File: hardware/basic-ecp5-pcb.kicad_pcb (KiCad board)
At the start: 4 copper layers, 100 x 68 mm, 75 parts, among them J1 Conn_01x02, J10 Conn_02x05_Odd_Even, J2 Conn_02x20_Odd_Even, J3 Conn_02x06_Odd_Even, J4 Conn_02x06_Odd_Even, J5 Conn_02x06_Odd_Even, J6 Conn_02x06_Odd_Even, J7 Conn_02x06_Odd_Even, J8 Conn_02x06_Odd_Even, J9 Conn_02x20_Odd_Even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

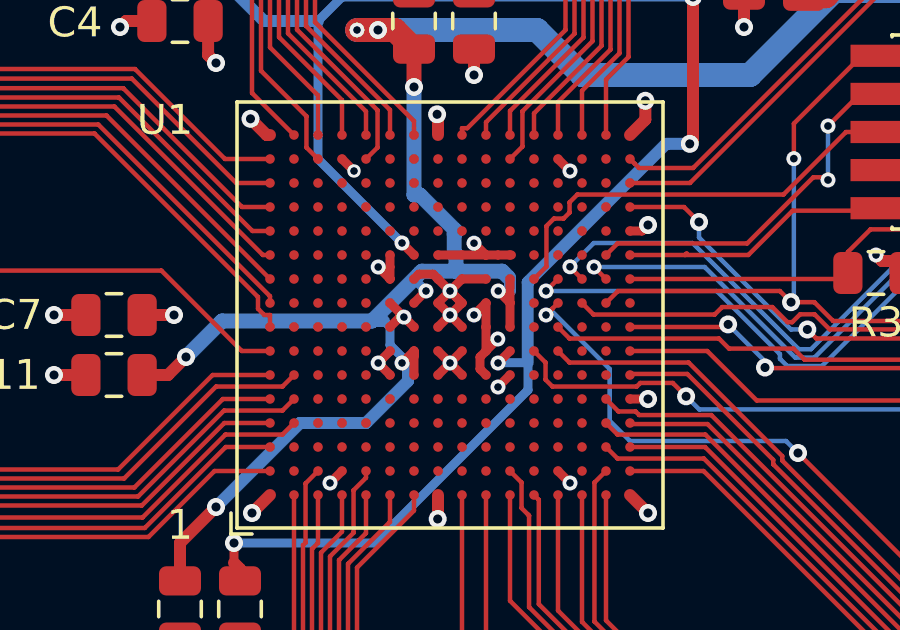
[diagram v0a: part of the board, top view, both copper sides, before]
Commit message: Fanout BGA center
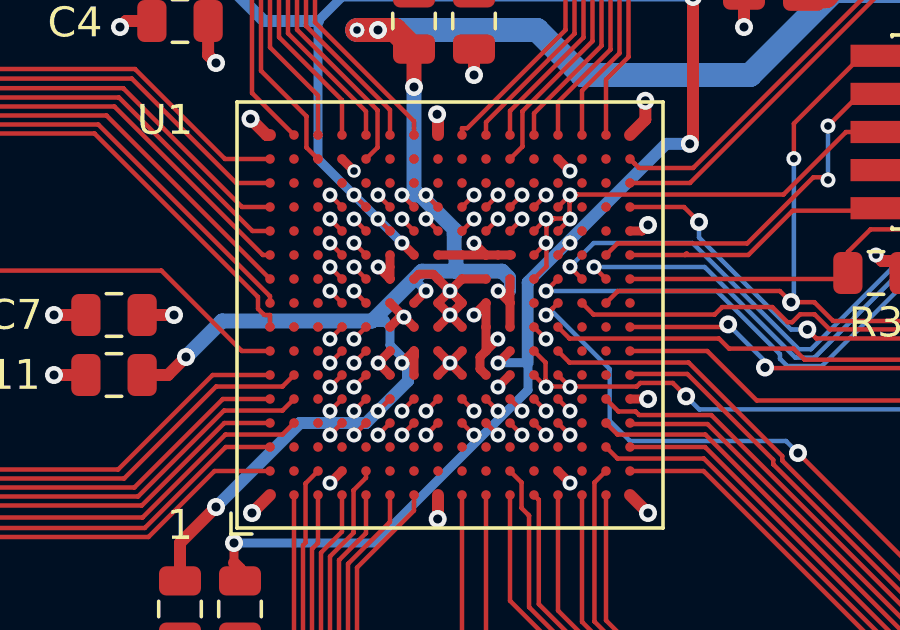
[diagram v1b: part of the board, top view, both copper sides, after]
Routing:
- net Net-(U1-PadN6): track 0.00 -> 0.57 mm, vias 0 -> 1
- net Net-(U1-PadN5): track 0.00 -> 0.57 mm, vias 0 -> 1
- net Net-(U1-PadN4): track 0.00 -> 0.57 mm, vias 0 -> 1
- net Net-(U1-PadN13): track 0.00 -> 0.57 mm, vias 0 -> 1
- net Net-(U1-PadN12): track 0.00 -> 0.57 mm, vias 0 -> 1
- net Net-(U1-PadN11): track 0.00 -> 0.57 mm, vias 0 -> 1
- net Net-(U1-PadM6): track 0.00 -> 0.57 mm, vias 0 -> 1
- net Net-(U1-PadM5): track 0.00 -> 0.57 mm, vias 0 -> 1
- net Net-(U1-PadM4): track 0.00 -> 0.57 mm, vias 0 -> 1
- net Net-(U1-PadM13): track 0.00 -> 0.57 mm, vias 0 -> 1
- net Net-(U1-PadM12): track 0.00 -> 0.57 mm, vias 0 -> 1
- net Net-(U1-PadM11): track 0.00 -> 0.57 mm, vias 0 -> 1
- net Net-(U1-PadL5): track 0.00 -> 0.57 mm, vias 0 -> 1
- net Net-(U1-PadL4): track 0.00 -> 0.57 mm, vias 0 -> 1
- net Net-(U1-PadL13): track 0.00 -> 0.57 mm, vias 0 -> 1
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
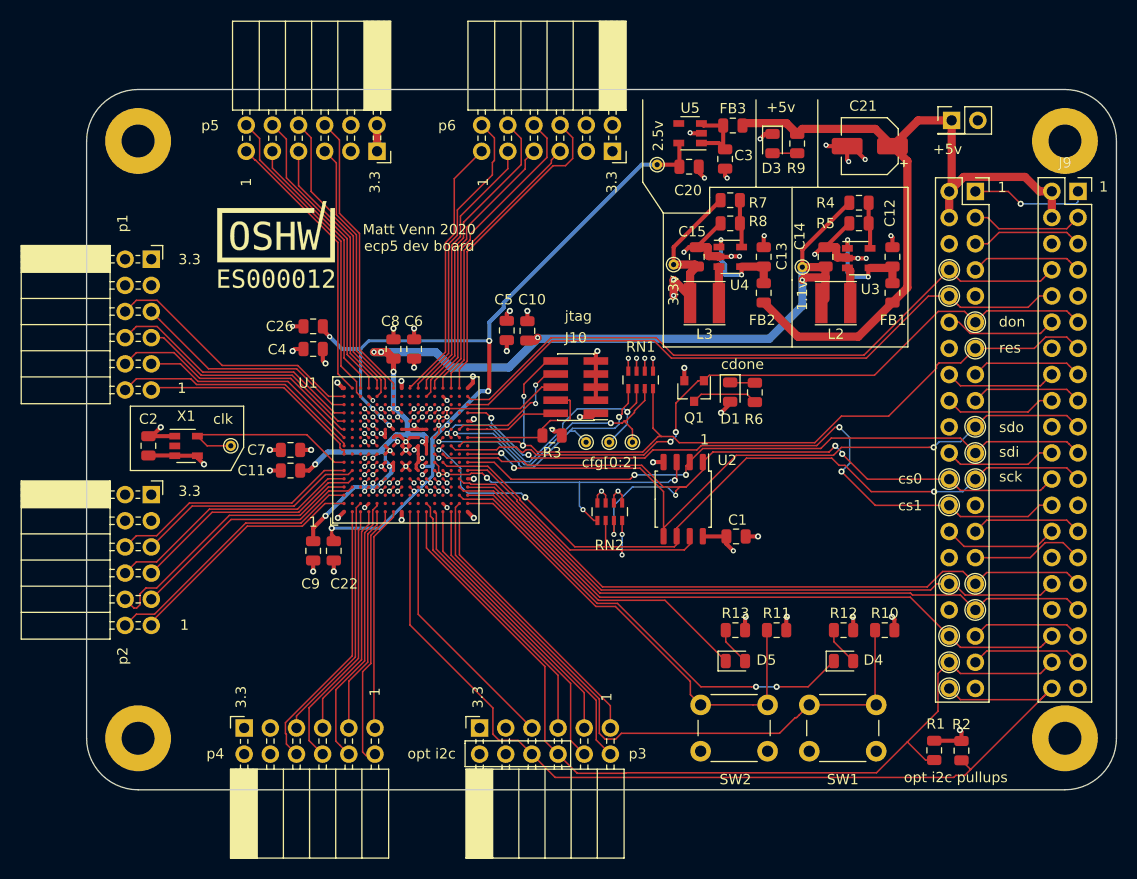
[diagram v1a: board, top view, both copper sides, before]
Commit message: Fanout BGA outer #1
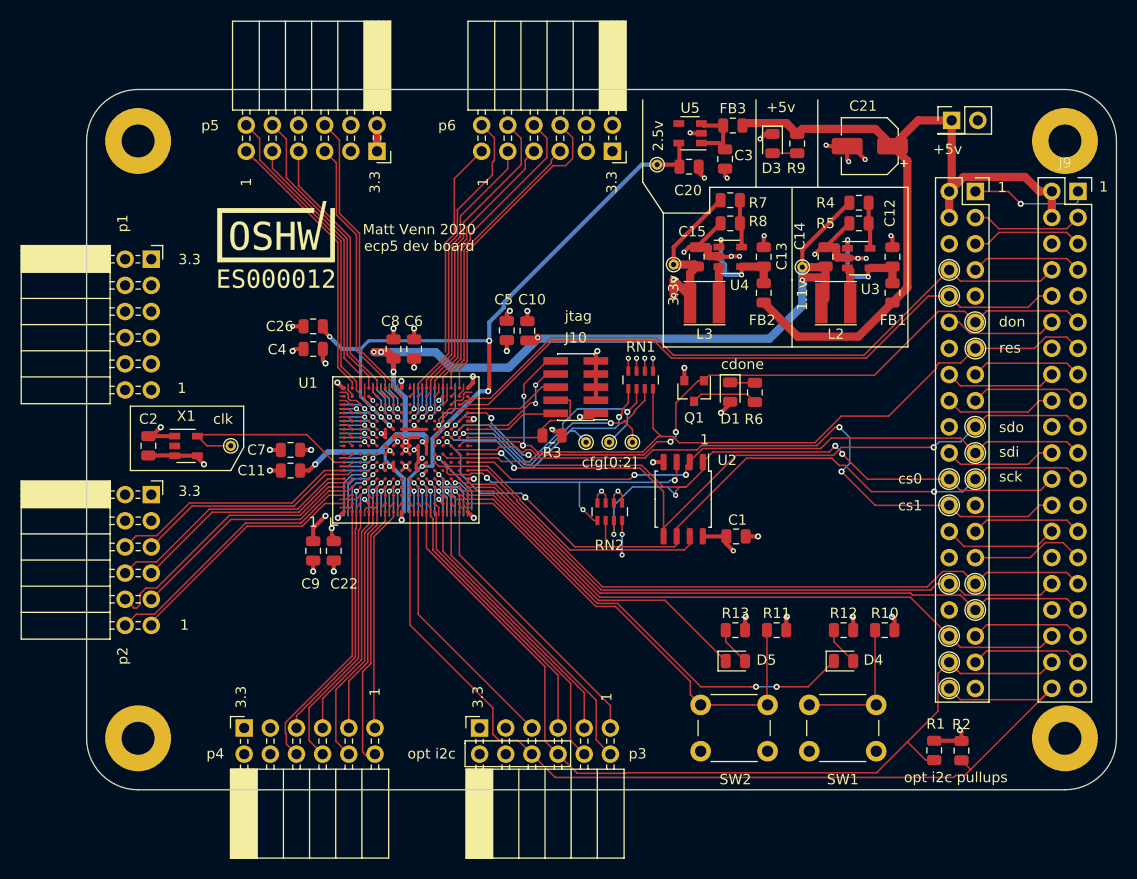
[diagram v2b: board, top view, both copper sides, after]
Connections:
- U1 pad E13: Net-(U1-PadE13) -> +2V5
- U1 pad F12: Net-(U1-PadF12) -> +2V5
- U1 pad N11: Net-(U1-PadN11) -> +2V5
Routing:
- net button1: track 64.1 -> 15.2 mm
- net p5_9: track 29.8 -> 1.37 mm
- net p1_10: track 25.6 -> 0.40 mm
- net p1_9: track 25.2 -> 0.40 mm
- net p1_8: track 24.8 -> 0.40 mm
- net p1_7: track 24.5 -> 0.40 mm
- net p1_4: track 22.5 -> 0.40 mm
- net p1_3: track 22.1 -> 0.40 mm
- net p1_1: track 22.0 -> 0.40 mm
- net p1_2: track 21.7 -> 0.40 mm
- net Net-(U1-PadM8): track 0.57 -> 6.89 mm
- net +2V5: track 87.2 -> 80.8 mm, vias 6 -> 9
- net Net-(U1-PadE6): track 0.57 -> 6.38 mm
- net Net-(U1-PadD6): track 0.57 -> 6.10 mm
- net +1V1: track 121.1 -> 115.8 mm
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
